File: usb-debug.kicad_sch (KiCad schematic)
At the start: 87 parts, among them IC1 NCP380LSNAJAAT1G, IC15 TPS7A0518P_SOT23-5, IC3 NCP380LSNAJAAT1G, IC5 FT232R_QFN, IC7 HD3SS3220RNH, J11 USB-C_WE_632723300011, J5 USB-Micro-B_Molex_473460001, J9 USB-Micro-B_Molex_473460001, T6 BSS138PW, T7 BSS138PW, T9 BSS138PW, U8 74LVC1G07_SOT-753

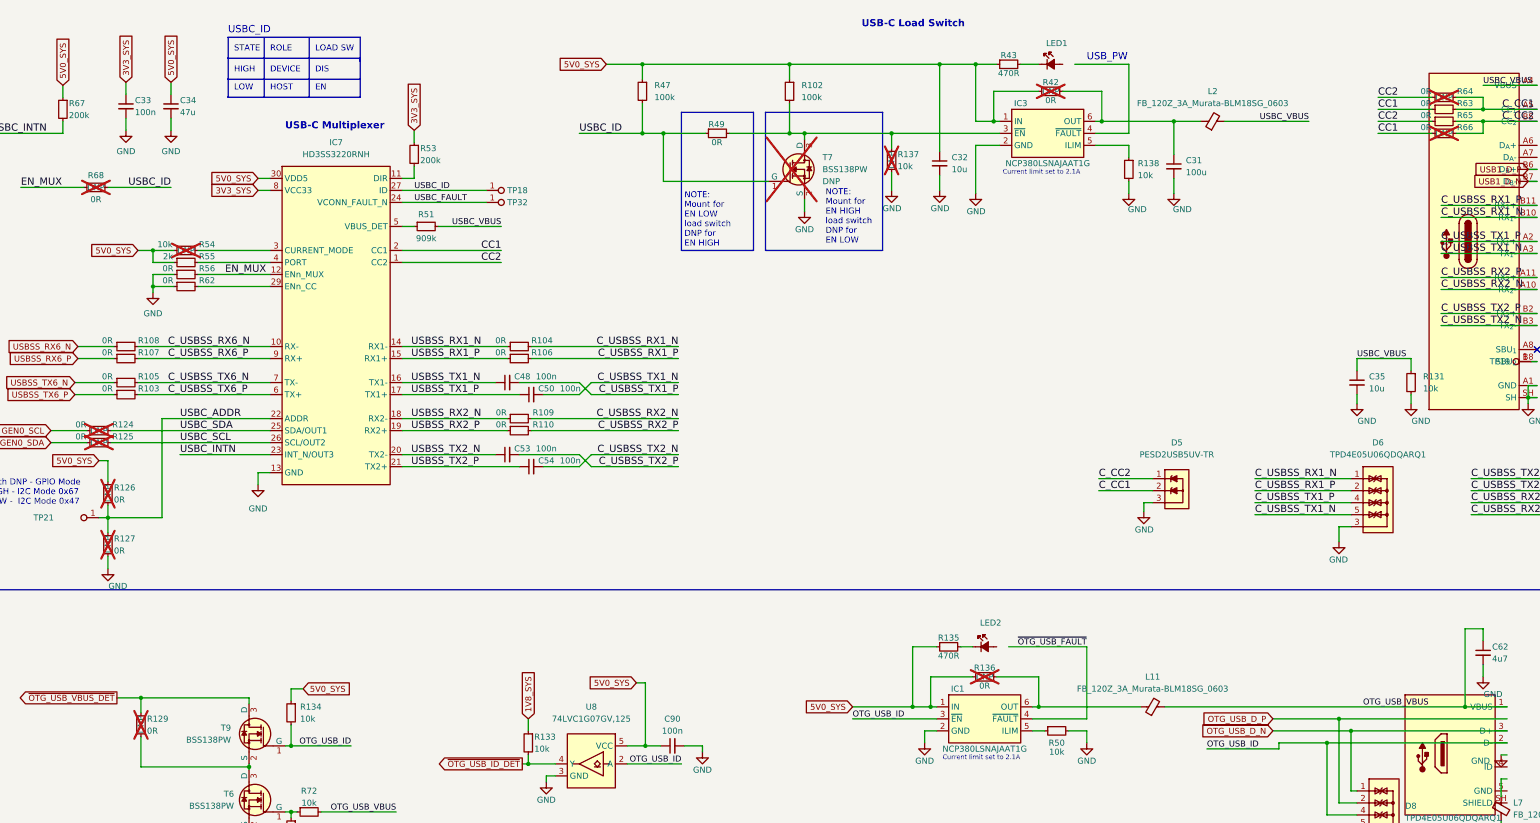
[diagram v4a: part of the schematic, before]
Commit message: [#83358] Run kmake dnp
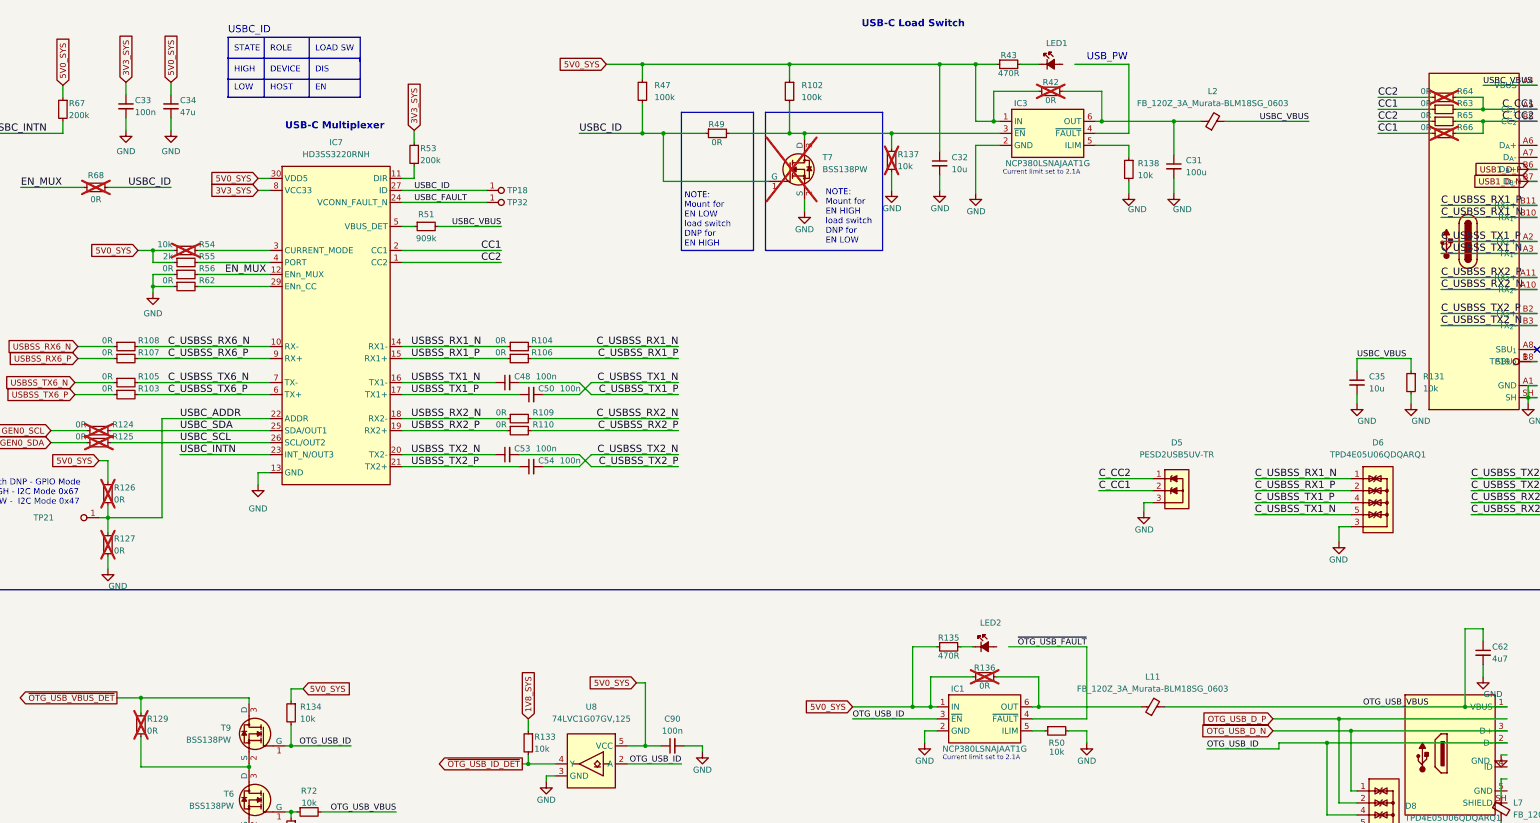
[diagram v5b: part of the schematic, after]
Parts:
- R124, R125, R126, R127, R129, R136, R137, R42, R54, R64, R66, R68, T7: DNP DNP -> (none)
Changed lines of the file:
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@@
 			)
 		)
-		(property "DNP" "DNP"
-			(at 218.44 59.0549 0)
-			(effects
-				(font
-					(size 1.27 1.27)
-				)
-				(justify left)
-			)
-		)
 		(property "Author" "Antmicro"
 			(at 229.87 80.645 0)
@@
 			)
 		)
-		(property "DNP" "DNP"
-			(at 83.82 73.66 0)
-			(effects
-				(font
-					(size 1.27 1.27)
-				)
-			)
-		)
 		(property "License" "Apache-2.0"
 			(at 101.6 99.06 0)
@@
 			)
 		)
-		(property "DNP" "DNP"
-			(at 64.77 60.325 0)
-			(effects
-				(font
-					(size 1.27 1.27)
-				)
-			)
-		)
 		(property "License" "Apache-2.0"
 			(at 82.55 85.725 0)
@@
 			)
 		)
-		(property "DNP" "DNP"
-			(at 349.885 41.275 0)
-			(effects
-				(font
-					(size 1.27 1.27)
-				)
-			)
-		)
 		(property "License" "Apache-2.0"
 			(at 367.665 66.675 0)
@@
 			)
 		)
-		(property "DNP" "DNP"
-			(at 349.885 48.895 0)
-			(effects
-				(font
-					(size 1.27 1.27)
-				)
-			)
-		)
 		(property "License" "Apache-2.0"
 			(at 367.665 74.295 0)
@@
 			)
 		)
-		(property "DNP" "DNP"
-			(at 266.7 40.005 0)
-			(effects
-				(font
-					(size 1.27 1.27)
-				)
-			)
-		)
 		(property "License" "Apache-2.0"
 			(at 284.48 14.605 0)
@@
 			)
 		)
-		(property "DNP" "DNP"
-			(at 233.045 52.705 0)
-			(effects
-				(font
-					(size 1.27 1.27)
-				)
-				(justify left)
-			)
-		)
 		(property "License" "Apache-2.0"
 			(at 207.645 72.39 0)
@@
 			)
 		)
-		(property "DNP" "DNP"
-			(at 67.31 123.19 0)
-			(effects
-				(font
-					(size 1.27 1.27)
-				)
-				(justify left)
-			)
-		)
 		(property "License" "Apache-2.0"
 			(at 41.91 142.875 0)
@@
 			)
 		)
-		(property "DNP" "DNP"
-			(at 74.295 172.085 0)
-			(effects
-				(font
-					(size 1.27 1.27)
-				)
-				(justify left)
-			)
-		)
 		(property "License" "Apache-2.0"
 			(at 48.895 191.77 0)
@@
 			)
 		)
-		(property "DNP" "DNP"
-			(at 65.405 111.76 0)
-			(effects
-				(font
-					(size 1.27 1.27)
-				)
-			)
-		)
 		(property "License" "Apache-2.0"
 			(at 83.185 137.16 0)
@@
 			)
 		)
-		(property "DNP" "DNP"
-			(at 67.31 133.985 0)
-			(effects
-				(font
-					(size 1.27 1.27)
-				)
-				(justify left)
-			)
-		)
 		(property "License" "Apache-2.0"
 			(at 41.91 153.67 0)
@@
 			)
 		)
-		(property "DNP" "DNP"
-			(at 65.405 114.3 0)
-			(effects
-				(font
-					(size 1.27 1.27)
-				)
-			)
-		)
 		(property "License" "Apache-2.0"
 			(at 83.185 139.7 0)
@@
 			(effects
 				(font
-					(size 1.27 1.27)
-				)
-			)
-		)
-		(property "DNP" "DNP"
-			(at 252.73 163.83 0)
-			(effects
-				(font

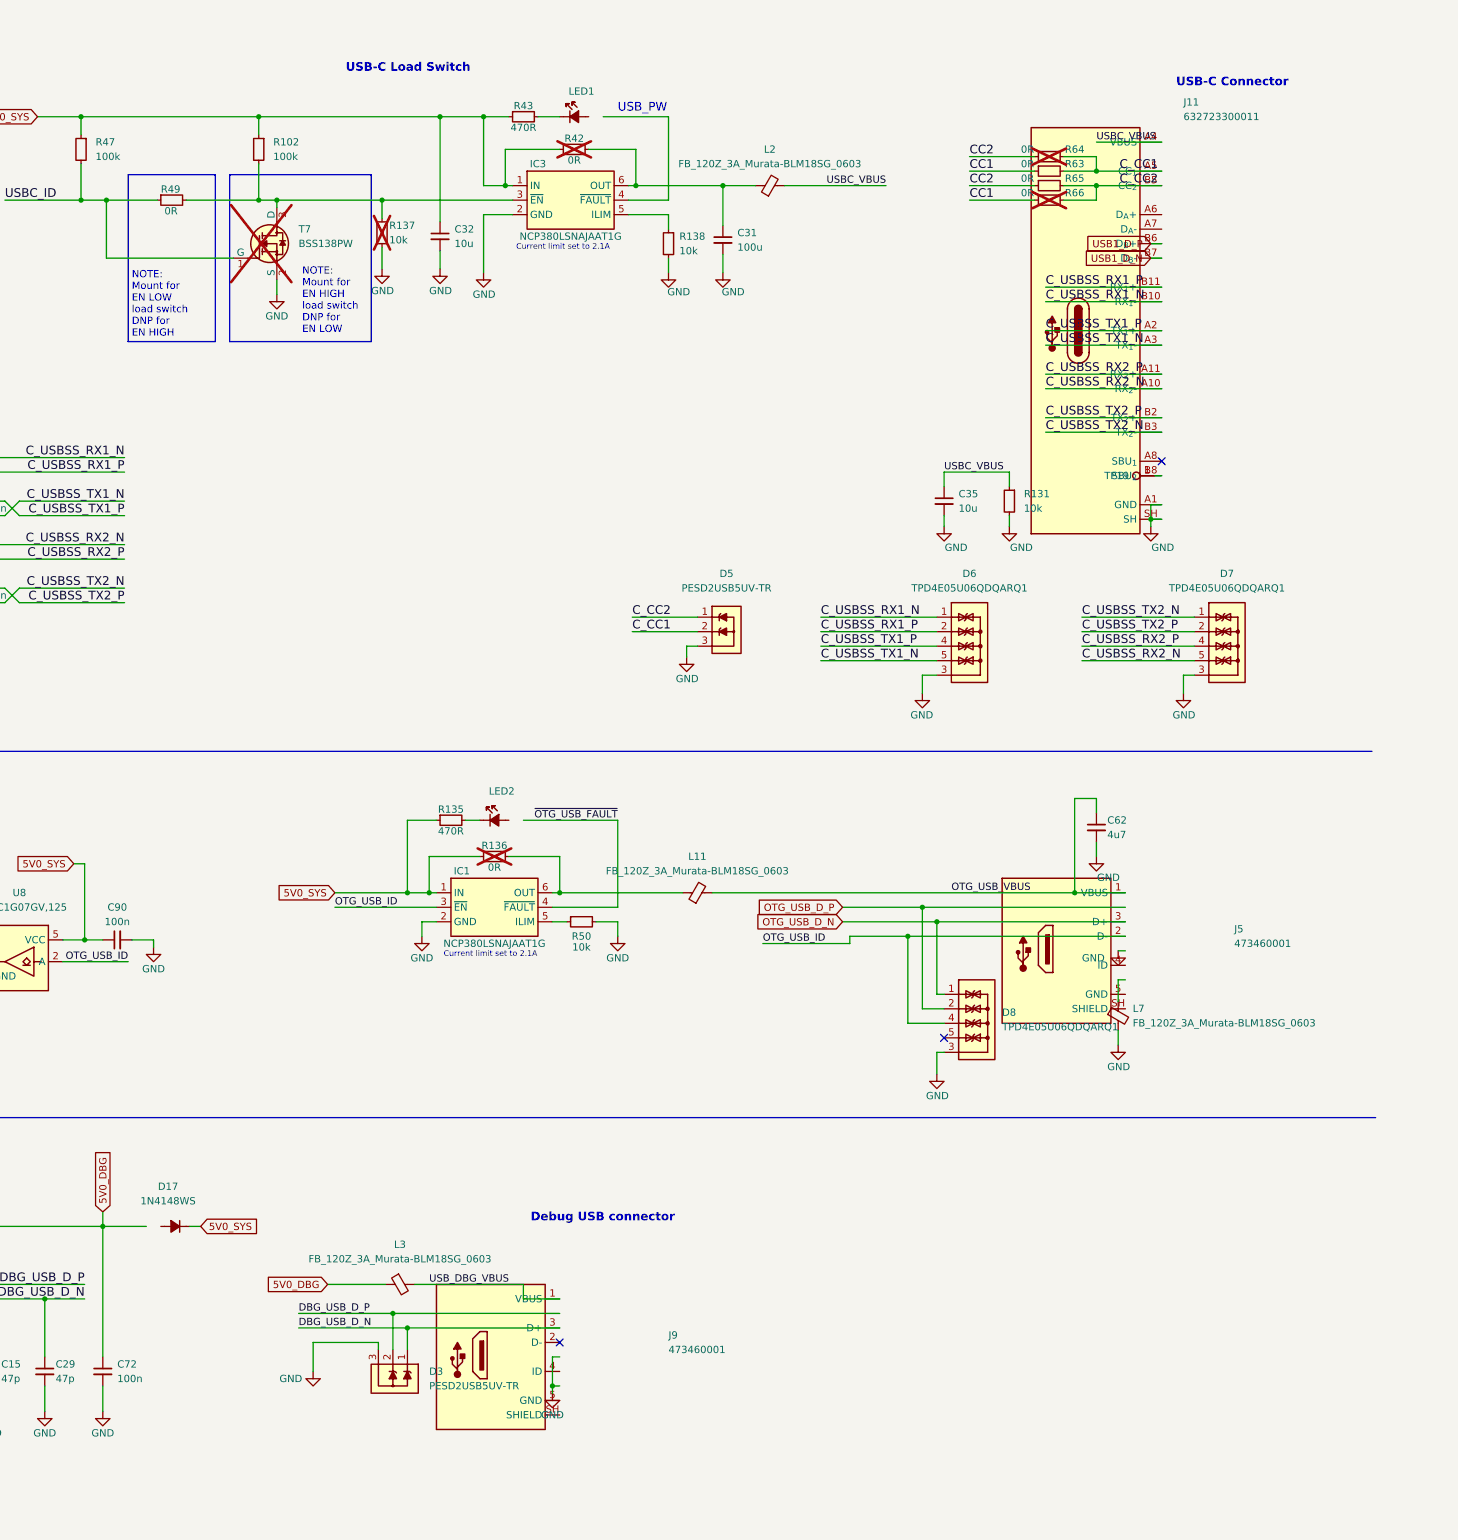
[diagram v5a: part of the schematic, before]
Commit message: [#83358] Repair broken symbol after update
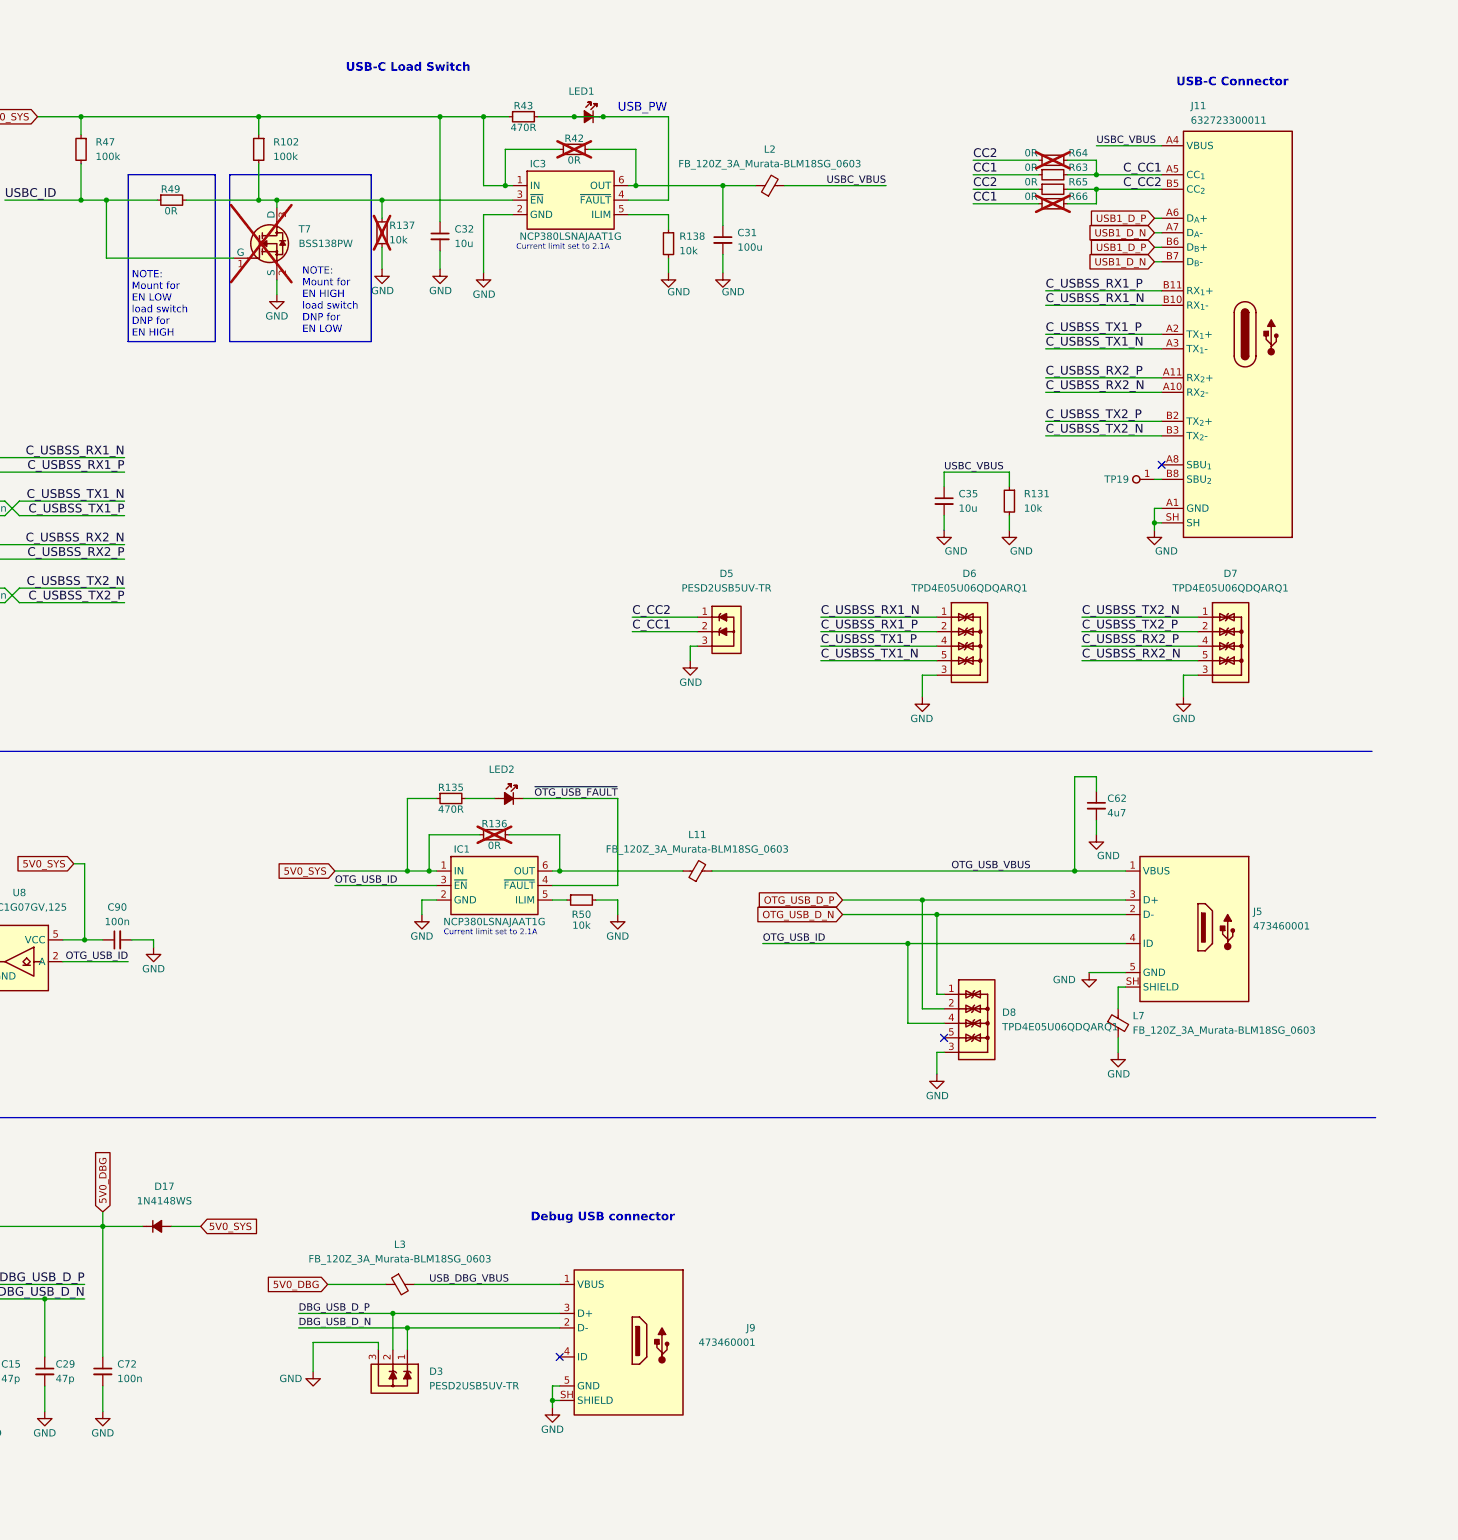
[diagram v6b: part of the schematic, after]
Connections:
- net 5V0_DBG: now also D17.1 (C)
- net 5V0_SYS: now also D17.2 (A); no longer D17.1 (C)
- net DBG_USB_D_N: now also J9.2 (D-); no longer J9.3 (D+)
- net DBG_USB_D_P: now also J9.3 (D+)
- net GND: now also J5.5 (GND), J9.5 (GND), J9.SH (SHIELD)
- net OTG_USB_D_N: now also J5.2 (D-); no longer J5.3 (D+)
- net OTG_USB_D_P: now also J5.3 (D+)
- net OTG_USB_ID: now also J5.4 (ID); no longer J5.2 (D-)
- net USB1_D_N: now also J11.A7 (D_{A}-)
- net USB1_D_P: now also J11.A6 (D_{A}+)
- net ~{OTG_USB_FAULT}: now also LED2.1 (C)
- net at L7.1: now also J5.SH (SHIELD)
- net at LED1.1 (C), R43.2: now also IC3.4 (~{FAULT}), LED1.2 (A)
- net at R135.2: now also LED2.2 (A); no longer LED2.1 (C)
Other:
- moved on the sheet: C62, D17, D7, IC1, J11, J5, J9, L11, L7, LED1, LED2, R135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
